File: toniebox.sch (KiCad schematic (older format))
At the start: 11 parts, among them U2 CC3200

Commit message: add led
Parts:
- added D10: LED_RGB, symbol Device:LED_RGB
- added R61, R62, R65: R, symbol Device:R
- added T4, T5, T6: Q_NMOS_GSD, symbol Device:Q_NMOS_GSD
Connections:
- net labels removed: TX1
- wire segments 47 -> 50
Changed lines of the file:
@@
 RX
 Text Label 5800 2600 0    50   ~ 0
-TX1
+TX
 Wire Wire Line
 	2500 7200 2150 7200
@@
 Wire Wire Line
 	2050 6050 2600 6050
+$Comp
+L Device:LED_RGB D10
+U 1 1 5E263FCE
+P 10400 4650
+F 0 "D10" H 10400 5147 50  0000 C CNN
+F 1 "LED_RGB" H 10400 5056 50  0000 C CNN
+F 2 "" H 10400 4600 50  0001 C CNN
+F 3 "~" H 10400 4600 50  0001 C CNN
+	1    10400 4650
+	1    0    0    -1
+$EndComp
+$Comp
+L Device:Q_NMOS_GSD T4
+U 1 1 5E26546C
+P 9300 6250
+F 0 "T4" H 9504 6296 50  0000 L CNN
+F 1 "Q_NMOS_GSD" H 9504 6205 50  0000 L CNN
+F 2 "" H 9500 6350 50  0001 C CNN
+F 3 "~" H 9300 6250 50  0001 C CNN
+	1    9300 6250
+	1    0    0    -1
+$EndComp
+$Comp
+L Device:Q_NMOS_GSD T5
+U 1 1 5E265922
+P 11300 6150
+F 0 "T5" H 11504 6196 50  0000 L CNN
+F 1 "Q_NMOS_GSD" H 11504 6105 50  0000 L CNN
+F 2 "" H 11500 6250 50  0001 C CNN
+F 3 "~" H 11300 6150 50  0001 C CNN
+	1    11300 6150
+	1    0    0    -1
+$EndComp
+$Comp
+L Device:R R61
+U 1 1 5E265F55
+P 9400 5650
+F 0 "R61" H 9470 5696 50  0000 L CNN
+F 1 "R" H 9470 5605 50  0000 L CNN
+F 2 "" V 9330 5650 50  0001 C CNN
+F 3 "~" H 9400 5650 50  0001 C CNN
+	1    9400 5650
+	1    0    0    -1
+$EndComp
+$Comp
+L Device:R R65
+U 1 1 5E26641D
+P 10400 5600
+F 0 "R65" H 10470 5646 50  0000 L CNN
+F 1 "R" H 10470 5555 50  0000 L CNN
+F 2 "" V 10330 5600 50  0001 C CNN
+F 3 "~" H 10400 5600 50  0001 C CNN
+	1    10400 5600
+	1    0    0    -1
+$EndComp
+$Comp
+L Device:R R62
+U 1 1 5E266529
+P 11400 5600
+F 0 "R62" H 11470 5646 50  0000 L CNN
+F 1 "R" H 11470 5555 50  0000 L CNN
+F 2 "" V 11330 5600 50  0001 C CNN
+F 3 "~" H 11400 5600 50  0001 C CNN
+	1    11400 5600
+	1    0    0    -1
+$EndComp
+Wire Wire Line
+	9400 5800 9400 6050
+$Comp
+L Device:Q_NMOS_GSD T6
+U 1 1 5E2687EE
+P 10300 6150
+F 0 "T6" H 10504 6196 50  0000 L CNN
+F 1 "Q_NMOS_GSD" H 10504 6105 50  0000 L CNN
+F 2 "" H 10500 6250 50  0001 C CNN
+F 3 "~" H 10300 6150 50  0001 C CNN
+	1    10300 6150
+	1    0    0    -1
+$EndComp
+Wire Wire Line
+	10400 5950 10400 5750
+Wire Wire Line
+	11400 5950 11400 5750
 $EndSCHEMATC

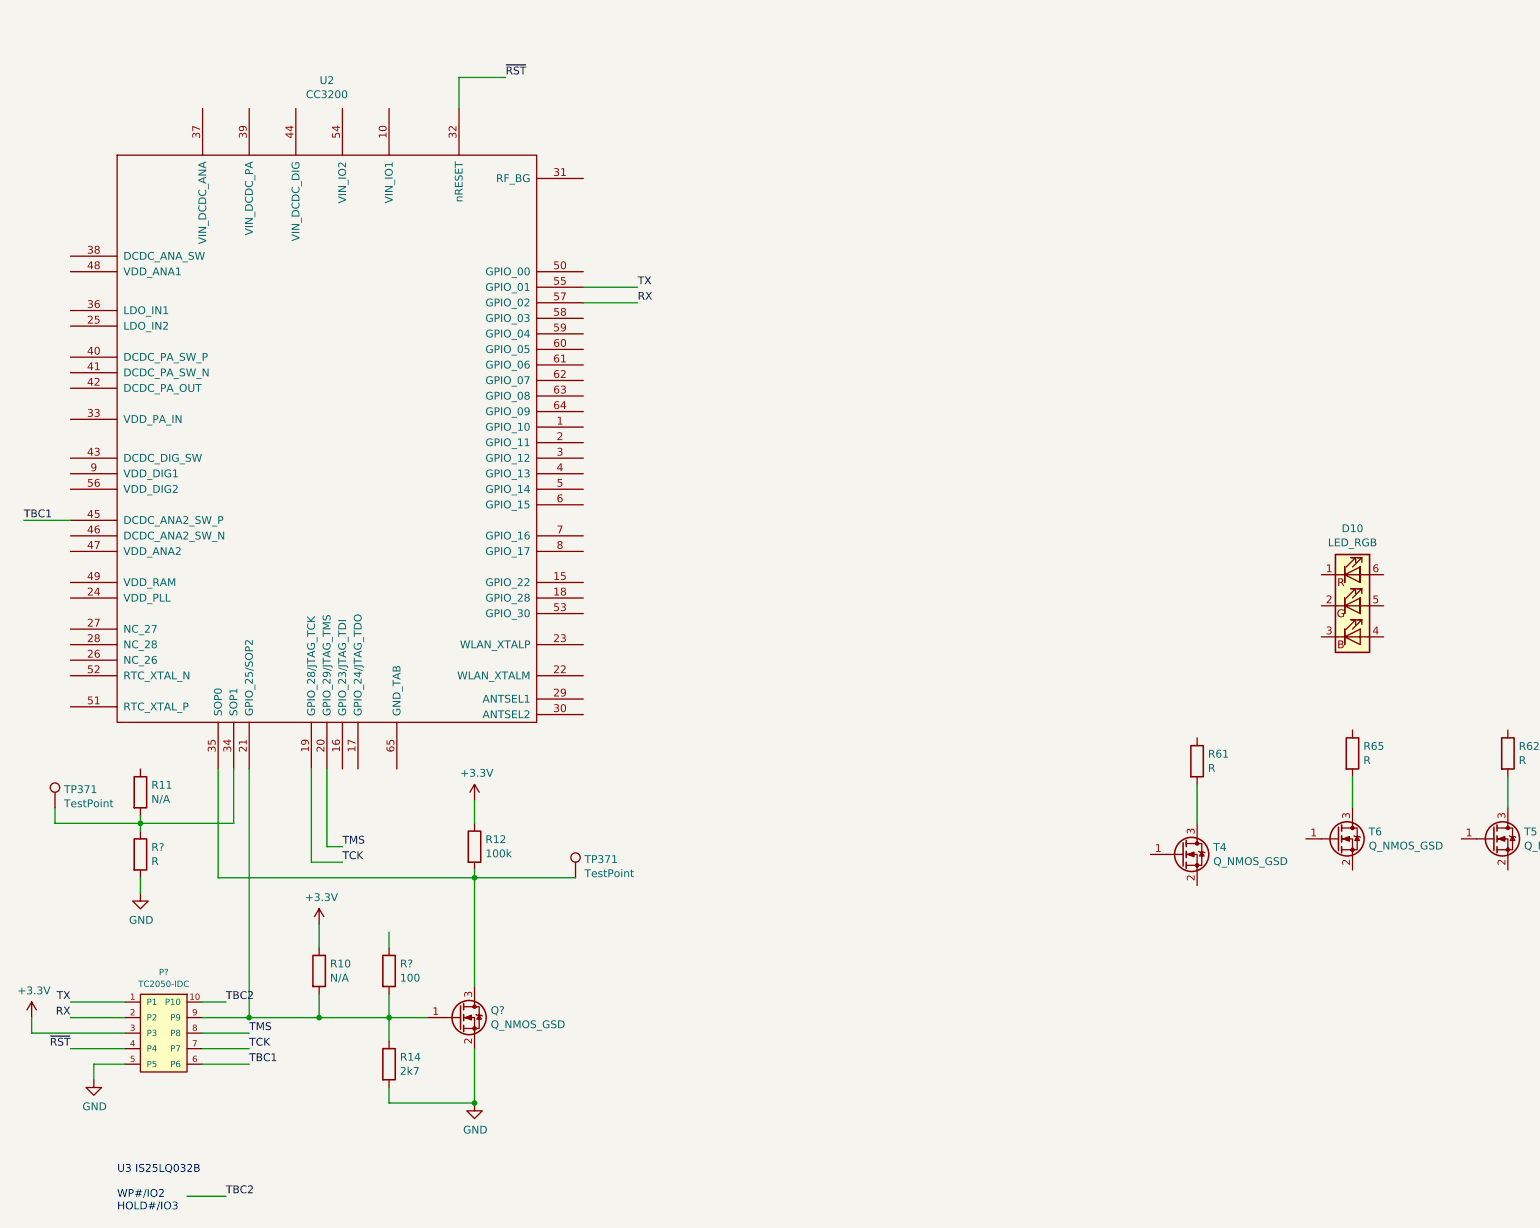
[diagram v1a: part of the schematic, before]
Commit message: adding testpoints
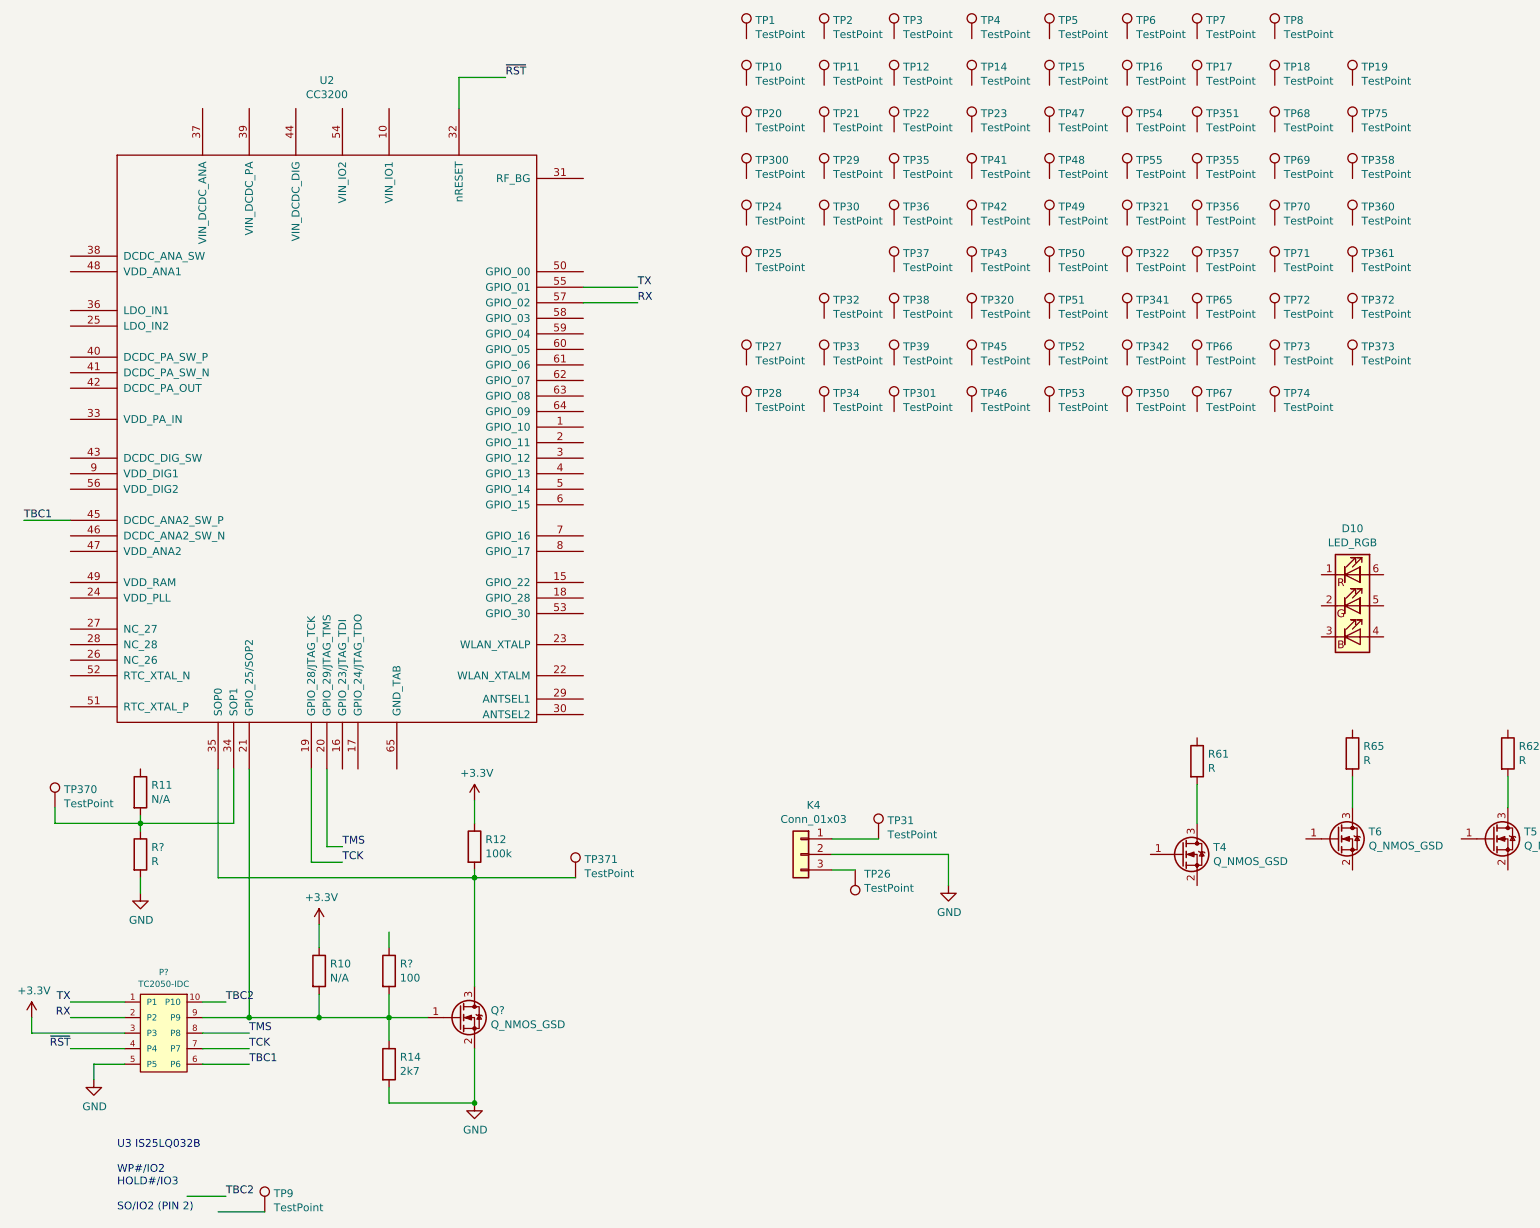
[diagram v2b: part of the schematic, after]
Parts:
- added K4: Conn_01x03, symbol Connector_Generic:Conn_01x03
- added TP1, TP10, TP11, TP12, TP14, TP15, TP16, TP17, TP18, TP19, TP2, TP20, TP21, TP22, TP23, TP24, TP25, TP26, TP27, TP28, TP29, TP3, TP30, TP300, TP301, TP31, TP32, TP320, TP321, TP322, TP33, TP34, TP341, TP342, TP35, TP350, TP351, TP355, TP356, TP357, TP358, TP36, TP360, TP361, TP37, TP372, TP373, TP38, TP39, TP4, TP41, TP42, TP43, TP45, TP46, TP47, TP48, TP49, TP5, TP50, TP51, TP52, TP53, TP54, TP55, TP6, TP65, TP66, TP67, TP68, TP69, TP7, TP70, TP71, TP72, TP73, TP74, TP75, TP8, TP9: TestPoint, symbol Connector:TestPoint
- renumbered TP371 to TP370
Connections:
- wire segments 50 -> 55
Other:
- note added: "U3 IS25LQ032B\n\nWP#/IO2\nHOLD#/IO3\n\nSO/IO2 (PIN 2)"
- note removed: "U3 IS25LQ032B\n\nWP#/IO2\nHOLD#/IO3"

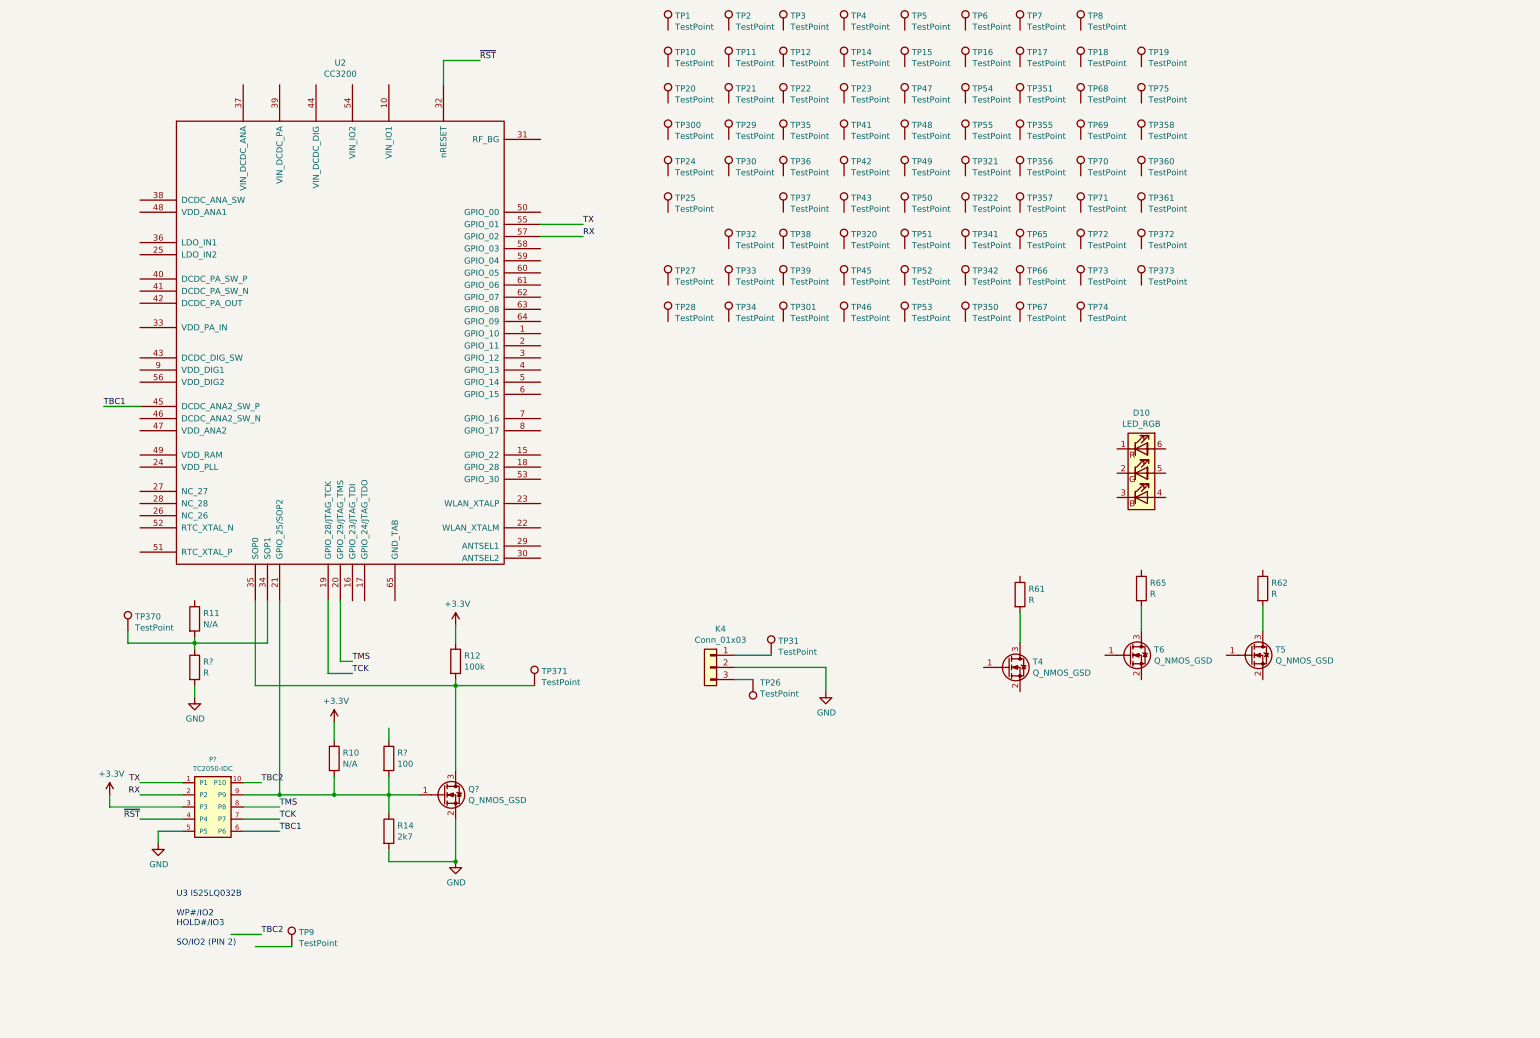
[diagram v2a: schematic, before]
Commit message: LED circuit, more testpoints
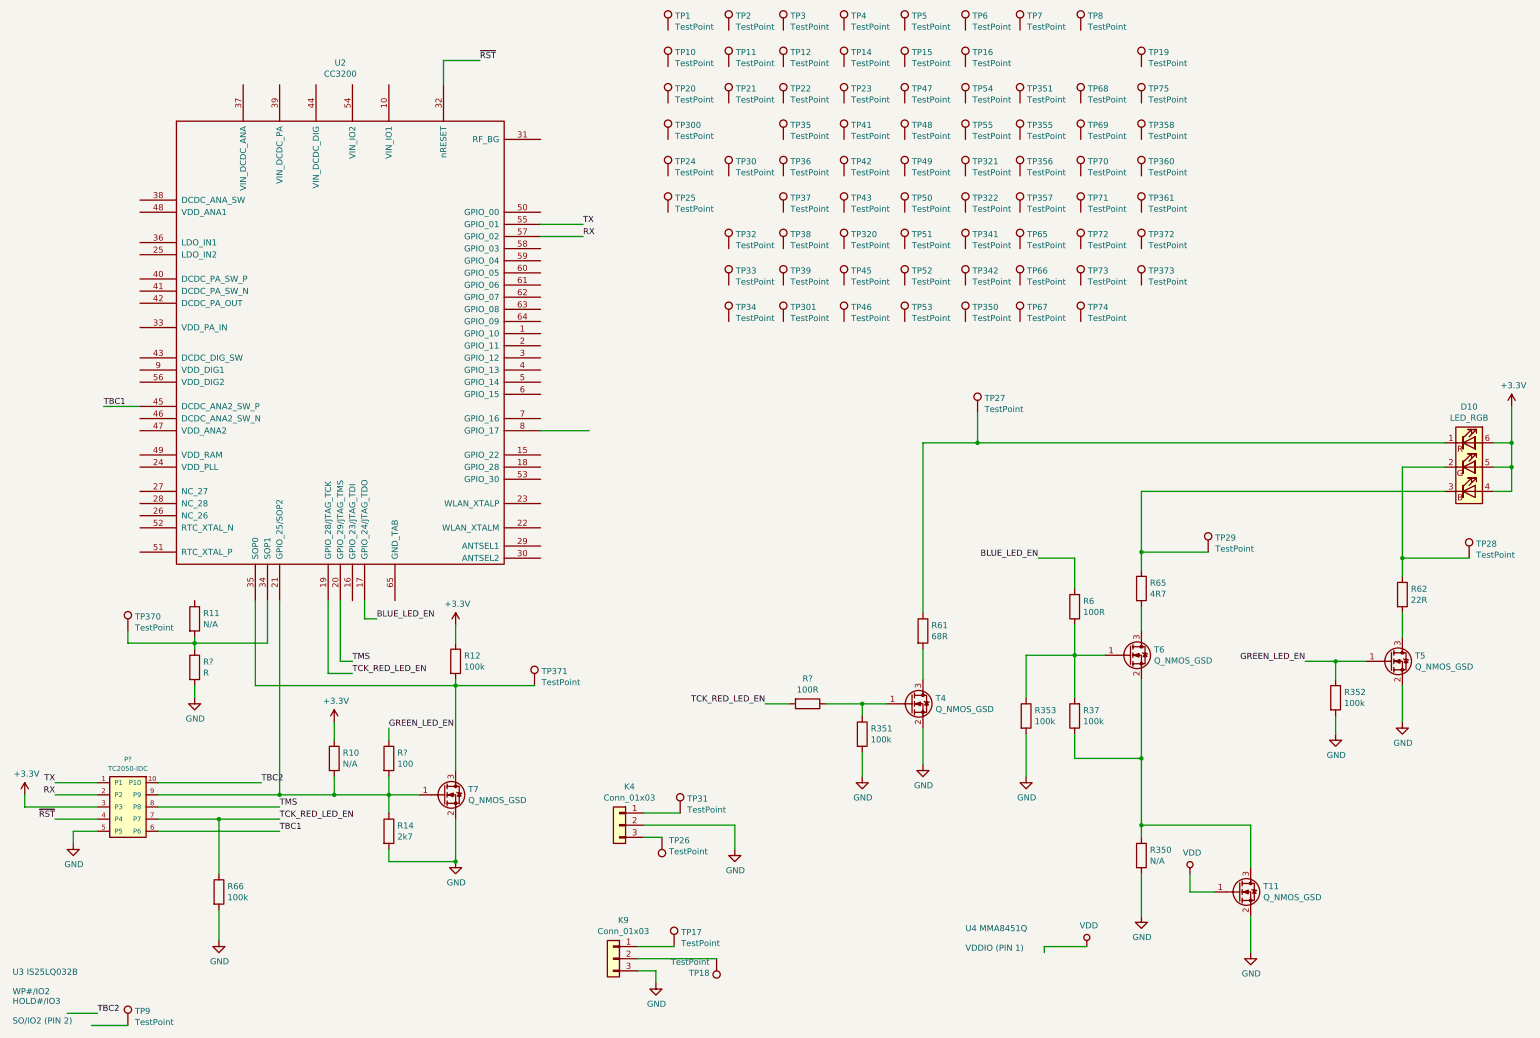
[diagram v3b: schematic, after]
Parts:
- added K9: Conn_01x03, symbol Connector_Generic:Conn_01x03
- added R350: N/A, symbol Device:R
- added R351, R352, R353, R37, R66: 100k, symbol Device:R
- added R6, R?: 100R, symbol Device:R
- added T11: Q_NMOS_GSD, symbol Device:Q_NMOS_GSD
- R61: value R -> 68R
- R62: value R -> 22R
- R65: value R -> 4R7
- gave numbers to parts that had none: 1
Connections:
- net labels added: BLUE_LED_EN, GREEN_LED_EN, TCK_RED_LED_EN, VDD
- net labels removed: TCK
- wire segments 55 -> 115
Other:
- note added: "U4 MMA8451Q\n\nVDDIO (PIN 1)"
- moved on the sheet: D10, K4, P?, R61, R62, T4, T5, TP17, TP18, TP26, TP27, TP28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
